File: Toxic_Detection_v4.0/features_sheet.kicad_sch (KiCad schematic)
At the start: 16 parts, among them IC1 ESP32-WROOM-32E-N16, J1 Conn_01x11_Pin, SW1 SW_Push

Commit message: feat: first placement (layout)
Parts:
- J1: footprint Connector_PinSocket_2.54mm:PinSocket_1x11_P2.54mm_Vertical -> Connector_PinHeader_2.54mm:PinHeader_1x11_P2.54mm_Vertical
- JP1: footprint Connector_PinSocket_2.54mm:PinSocket_1x03_P2.54mm_Vertical -> Connector_PinHeader_2.54mm:PinHeader_1x03_P2.54mm_Vertical
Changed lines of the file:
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@@
 		(title "Toxic_Detection_PCB")
 		(date "2026-02-12")
-		(rev "4.0")
+		(rev "4.1")
 		(company "Company: LNIS")
 		(comment 4 "Author: Paul Capgras")
@@
 			)
 		)
-		(property "Footprint" "Connector_PinSocket_2.54mm:PinSocket_1x11_P2.54mm_Vertical"
+		(property "Footprint" "Connector_PinHeader_2.54mm:PinHeader_1x11_P2.54mm_Vertical"
 			(at 36.83 120.65 0)
 			(effects
@@
 			)
 		)
-		(property "Footprint" "Connector_PinSocket_2.54mm:PinSocket_1x03_P2.54mm_Vertical"
+		(property "Footprint" "Connector_PinHeader_2.54mm:PinHeader_1x03_P2.54mm_Vertical"
 			(at 33.02 83.82 0)
 			(effects

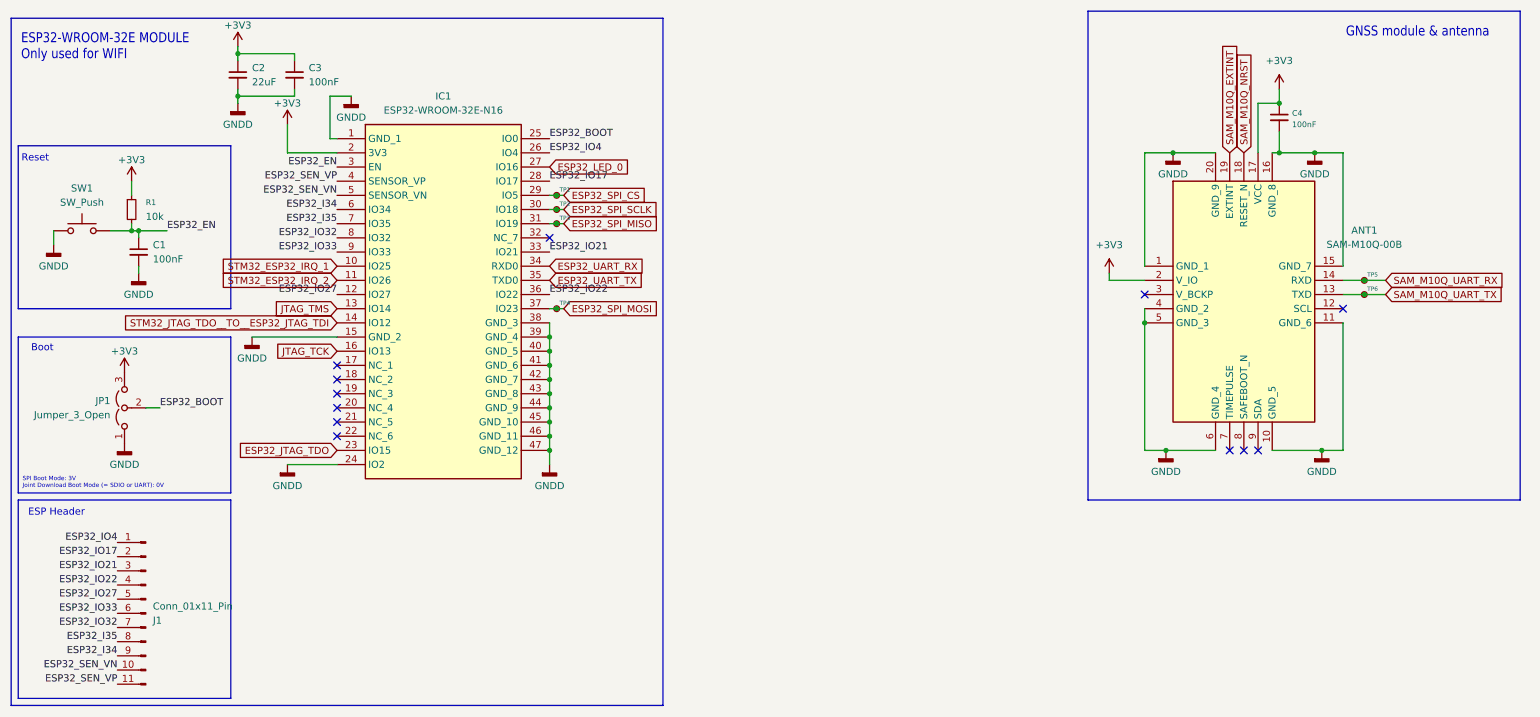
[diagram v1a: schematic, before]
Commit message: feat (layout) : finish routing, fill zones, and create custom footprints for some components
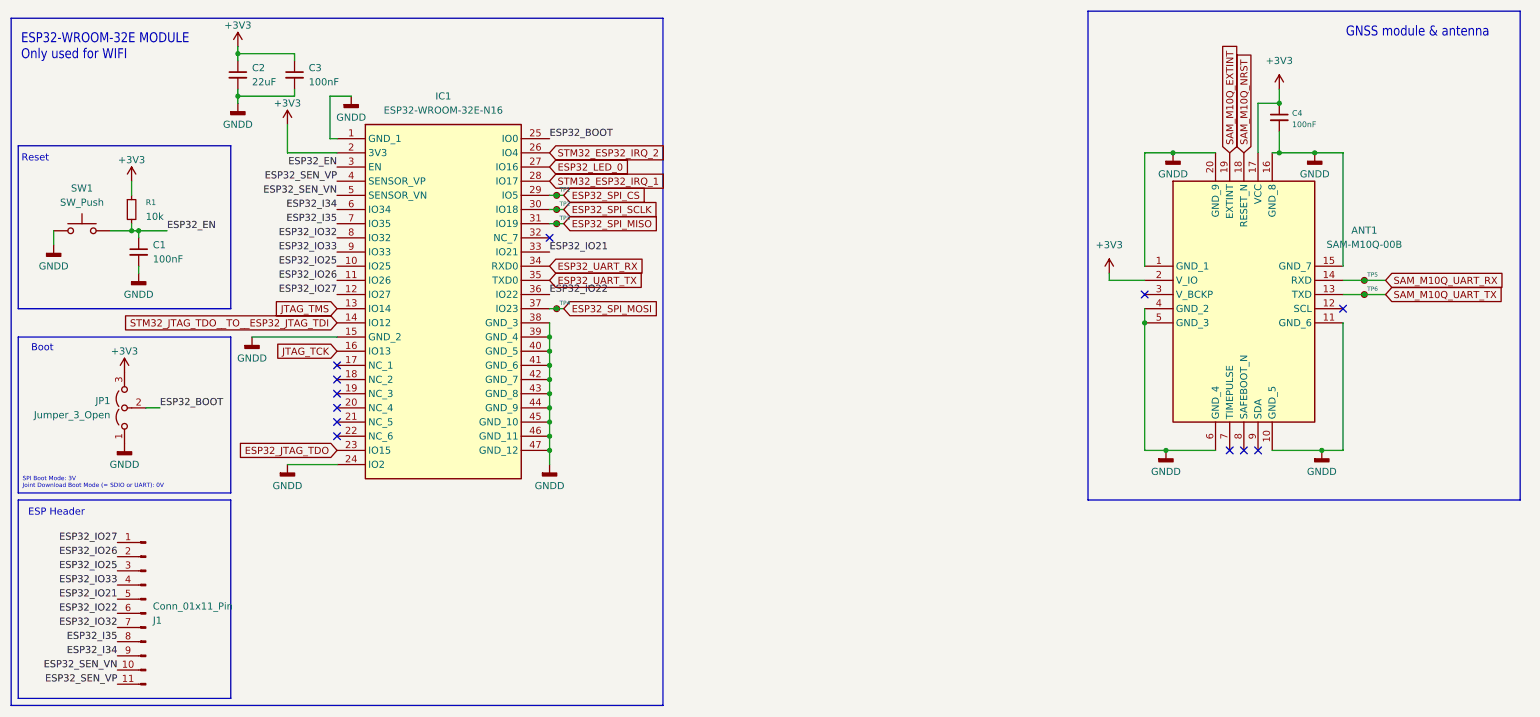
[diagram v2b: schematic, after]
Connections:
- net ESP32_IO21: now also J1.5 (Pin_5); no longer J1.3 (Pin_3)
- net ESP32_IO22: now also J1.6 (Pin_6); no longer J1.4 (Pin_4)
- net ESP32_IO27: now also J1.1 (Pin_1); no longer J1.5 (Pin_5)
- net ESP32_IO33: now also J1.4 (Pin_4); no longer J1.6 (Pin_6)
- net STM32_ESP32_IRQ_1: now also IC1.28 (IO17); no longer IC1.10 (IO25)
- net STM32_ESP32_IRQ_2: now also IC1.26 (IO4); no longer IC1.11 (IO26)
- net ESP32_IO17 renamed ESP32_IO26
- net ESP32_IO26: now also IC1.11 (IO26); no longer IC1.28 (IO17)
- removed net ESP32_IO4: IC1.26 (IO4), J1.1 (Pin_1)
- new net ESP32_IO25: IC1.10 (IO25), J1.3 (Pin_3)
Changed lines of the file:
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@@
-		)
-	)
-	(label "ESP32_IO27"
-		(at 31.75 118.11 180)
-		(effects
-			(font
-				(size 1.27 1.27)
-			)
-			(justify right bottom)
 		)
 	)
@@
 		)
 	)
-	(label "ESP32_IO21"
-		(at 31.75 113.03 180)
-		(effects
-			(font
-				(size 1.27 1.27)
-			)
-			(justify right bottom)
-		)
-	)
 	(label "ESP32_SEN_VN"
 		(at 71.12 45.72 180)
@@
 		)
 	)
+	(label "ESP32_IO26"
+		(at 71.12 60.96 180)
+		(effects
+			(font
+				(size 1.27 1.27)
+			)
+			(justify right bottom)
+		)
+	)
 	(label "ESP32_IO32"
 		(at 31.75 123.19 180)
@@
 		)
 	)
-	(label "ESP32_IO4"
-		(at 31.75 107.95 180)
-		(effects
-			(font
-				(size 1.27 1.27)
-			)
-			(justify right bottom)
-		)
-	)
 	(label "ESP32_SEN_VN"
 		(at 31.75 130.81 180)
@@
 		)
 	)
+	(label "ESP32_IO22"
+		(at 31.75 120.65 180)
+		(effects
+			(font
+				(size 1.27 1.27)
+			)
+			(justify right bottom)
+		)
+	)
 	(label "ESP32_EN"
 		(at 71.12 40.64 180)
@@
 		)
 	)
-	(label "ESP32_IO33"
-		(at 31.75 120.65 180)
-		(effects
-			(font
-				(size 1.27 1.27)
-			)
-			(justify right bottom)
-		)
-	)
-	(label "ESP32_IO17"
-		(at 31.75 110.49 180)
-		(effects
-			(font
-				(size 1.27 1.27)
-			)
-			(justify right bottom)
-		)
-	)
 	(label "ESP32_IO32"
 		(at 71.12 53.34 180)
@@
 		)
 	)
-	(label "ESP32_IO4"
-		(at 109.22 38.1 0)
-		(effects
-			(font
-				(size 1.27 1.27)
-			)
-			(justify left bottom)
+	(label "ESP32_IO25"
+		(at 31.75 113.03 180)
+		(effects
+			(font
+				(size 1.27 1.27)
+			)
+			(justify right bottom)
+		)
+	)
+	(label "ESP32_IO33"
+		(at 31.75 115.57 180)
+		(effects
+			(font
+				(size 1.27 1.27)
+			)
+			(justify right bottom)
 		)
 	)
@@
 		)
 	)
+	(label "ESP32_IO27"
+		(at 31.75 107.95 180)
+		(effects
+			(font
+				(size 1.27 1.27)
+			)
+			(justify right bottom)
+		)
+	)
 	(label "ESP32_BOOT"
 		(at 39.37 83.82 0)
@@
 		)
 	)
-	(label "ESP32_IO17"
-		(at 109.22 43.18 0)
-		(effects
-			(font
-				(size 1.27 1.27)
-			)
-			(justify left bottom)
-		)
-	)
 	(label "ESP32_IO27"
 		(at 71.12 63.5 180)
@@
 		)
 	)
+	(label "ESP32_IO26"
+		(at 31.75 110.49 180)
+		(effects
+			(font
+				(size 1.27 1.27)
+			)
+			(justify right bottom)
+		)
+	)
 	(label "ESP32_BOOT"
 		(at 109.22 35.56 0)
@@
 		)
 	)
-	(label "ESP32_IO22"
-		(at 31.75 115.57 180)
+	(label "ESP32_IO25"
+		(at 71.12 58.42 180)
 		(effects
 			(font
@@
 		)
 	)
+	(label "ESP32_IO21"
+		(at 31.75 118.11 180)
+		(effects
+			(font
+				(size 1.27 1.27)
+			)
+			(justify right bottom)
+		)
+	)
+	(global_label "STM32_ESP32_IRQ_1"
+		(shape input)
+		(at 109.22 43.18 0)
+		(fields_autoplaced yes)
+		(effects
+			(font
+				(size 1.27 1.27)
+			)
+			(justify left)
+		)
+		(property "Intersheetrefs" "${INTERSHEET_REFS}"
+			(at 131.6178 43.18 0)
+			(effects
+				(font
+					(size 1.27 1.27)
+				)
+				(justify left)
+				(hide yes)
+			)
+		)
+	)
 	(global_label "ESP32_UART_RX"
 		(shape input)
@@
 		)
 	)
+	(global_label "STM32_ESP32_IRQ_2"
+		(shape input)
+		(at 109.22 38.1 0)
+		(fields_autoplaced yes)
+		(effects
+			(font
+				(size 1.27 1.27)
+			)
+			(justify left)
+		)
+		(property "Intersheetrefs" "${INTERSHEET_REFS}"
+			(at 131.6178 38.1 0)
+			(effects
+				(font
+					(size 1.27 1.27)
+				)
+				(justify left)
+				(hide yes)
+			)
+		)
+	)
 	(global_label "ESP32_LED_0"
 		(shape input)
@@
 				(hide yes)
 			)
-		)
-	)
-	(global_label "STM32_ESP32_IRQ_1"
-		(shape input)
-		(at 71.12 58.42 180)
-		(fields_autoplaced yes)
-		(effects
-			(font
-				(size 1.27 1.27)
-			)
-			(justify right)
-		)
-		(property "Intersheetrefs" "${INTERSHEET_REFS}"
-			(at 48.7222 58.42 0)
-			(effects
-				(font
-					(size 1.27 1.27)
-				)
-				(justify right)
-				(hide yes)
-			)
-		)
-	)
-	(global_label "STM32_ESP32_IRQ_2"
-		(shape input)
-		(at 71.12 60.96 180)
-		(fields_autoplaced yes)
-		(effects
-			(font
-				(size 1.27 1.27)
-			)
-			(justify right)
-		)
-		(property "Intersheetrefs" "${INTERSHEET_REFS}"
-			(at 48.7222 60.96 0)
-			(effects
-				(font
-					(size 1.27 1.27)
-				)
-				(justify right)
-				(hide yes)
-			)
